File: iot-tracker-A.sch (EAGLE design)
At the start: 22 parts, among them U1 ESP-WROOM-02, U2 TPL5111DDCR, U3 MCP1640T-I_CHY

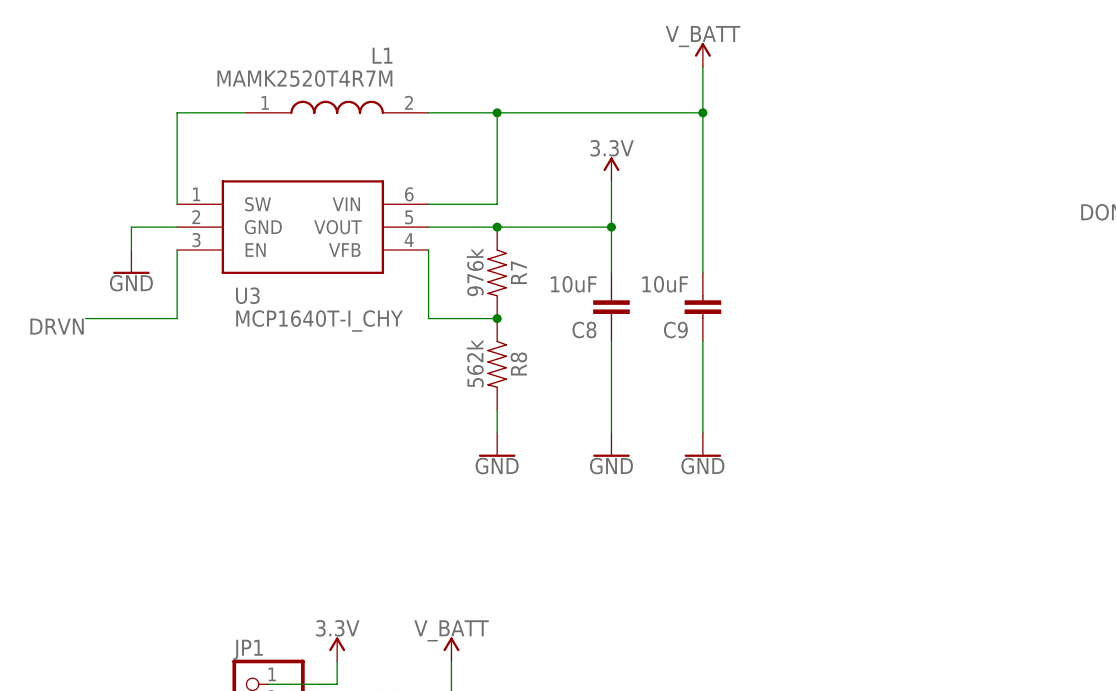
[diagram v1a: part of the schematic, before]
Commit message: Started phasing out the MCP1640 boost converter
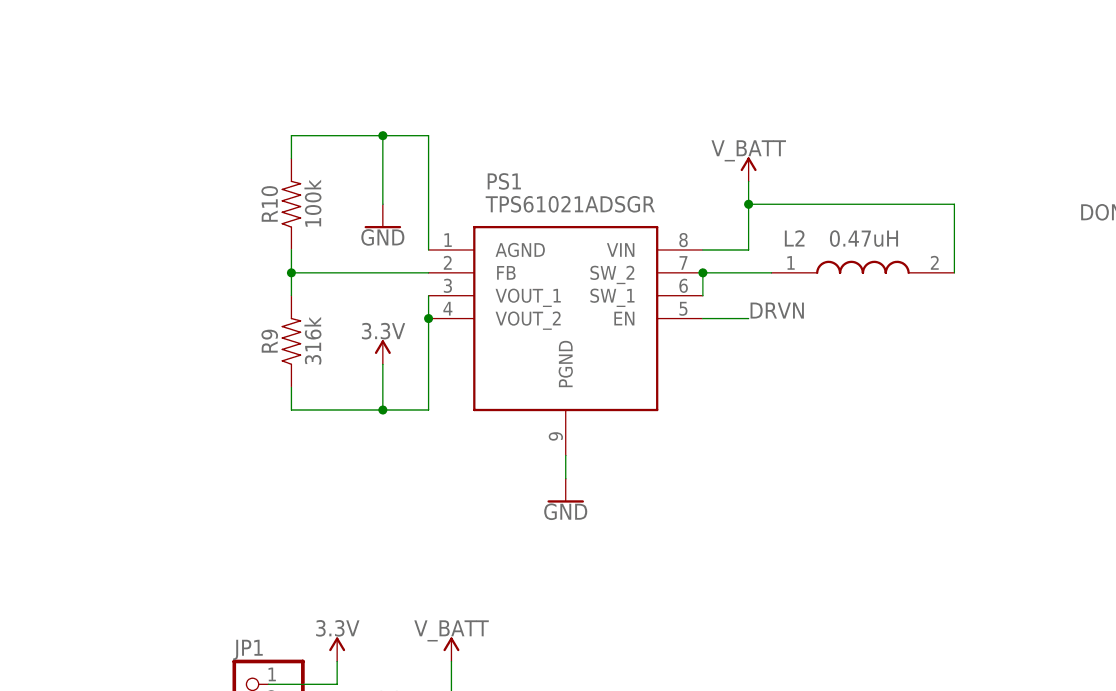
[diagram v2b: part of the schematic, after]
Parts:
- removed C8, C9: 10uF, SparkFun-Capacitors:10UF-0603-6.3V-20%
- removed L1: MAMK2520T4R7M, MAMK2520T4R7M:MAMK2520T4R7M
- removed R7: 976k, SparkFun-Resistors:680OHM-0603-1/10W-5%
- removed R8: 562k, SparkFun-Resistors:680OHM-0603-1/10W-5%
- removed U3: MCP1640T-I_CHY, MCP1640T-I_CHY:MCP1640T-I_CHY
- added L2: 0.47uH, IOT-Tracker-A:DFE252012P-R47M=P2
- added PS1: TPS61021ADSGR, IOT-Tracker-A:TPS61021ADSGR
- added R10: 100k, SparkFun-Resistors:100KOHM-0603-1/10W-1%
- added R9: 316k, SparkFun-Resistors:300KOHM-0603-1/10W-1%
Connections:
- removed net SW: L1.1, U3.SW
- removed net VFB: R7.2, R8.1, U3.VFB
- new net N$1: PS1.FB, R10.1, R9.2
- new net N$3: L2.1, PS1.SW_1, PS1.SW_2
- net 3.3V: now also PS1.VOUT_1, PS1.VOUT_2, R9.1; no longer C8.2, R7.1, U3.VOUT
- net DRVN: now also PS1.EN; no longer U3.EN
- net GND: now also PS1.AGND, PS1.PGND, R10.2; no longer C8.1, C9.1, R8.2, U3.GND
- net V_BATT: now also L2.2, PS1.VIN; no longer C9.2, L1.2, U3.VIN

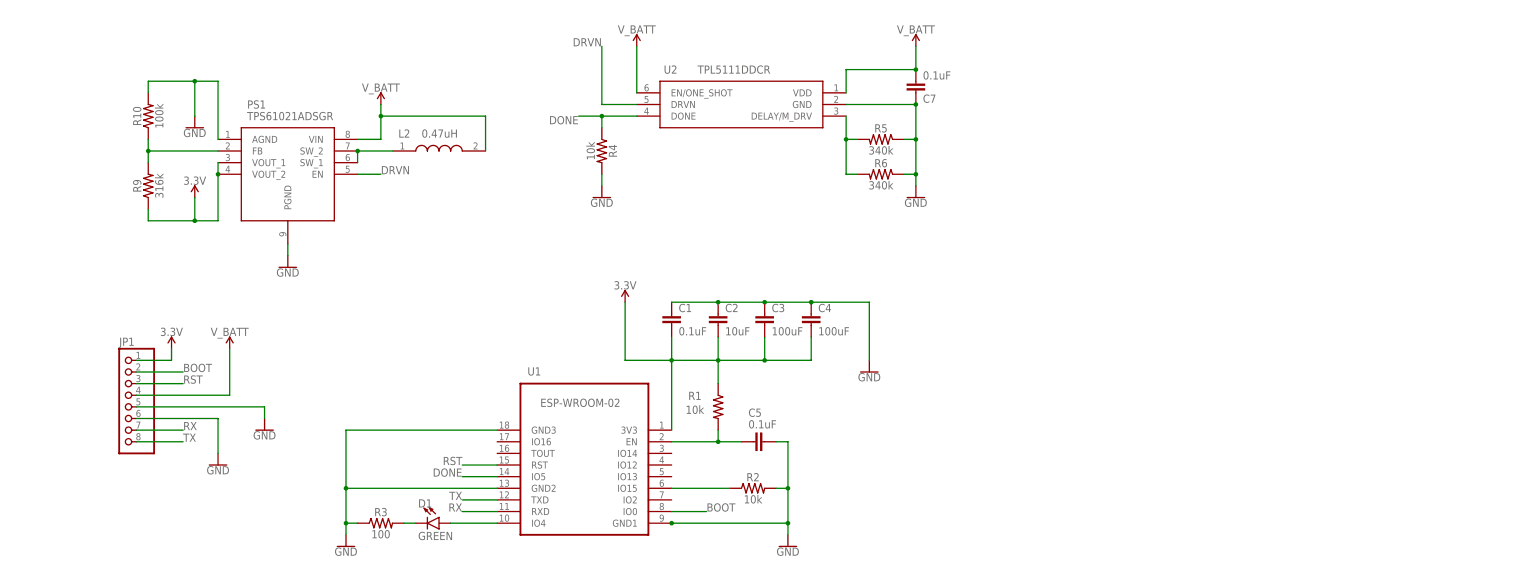
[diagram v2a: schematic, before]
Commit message: Integrated the TPS61021A into the schematic
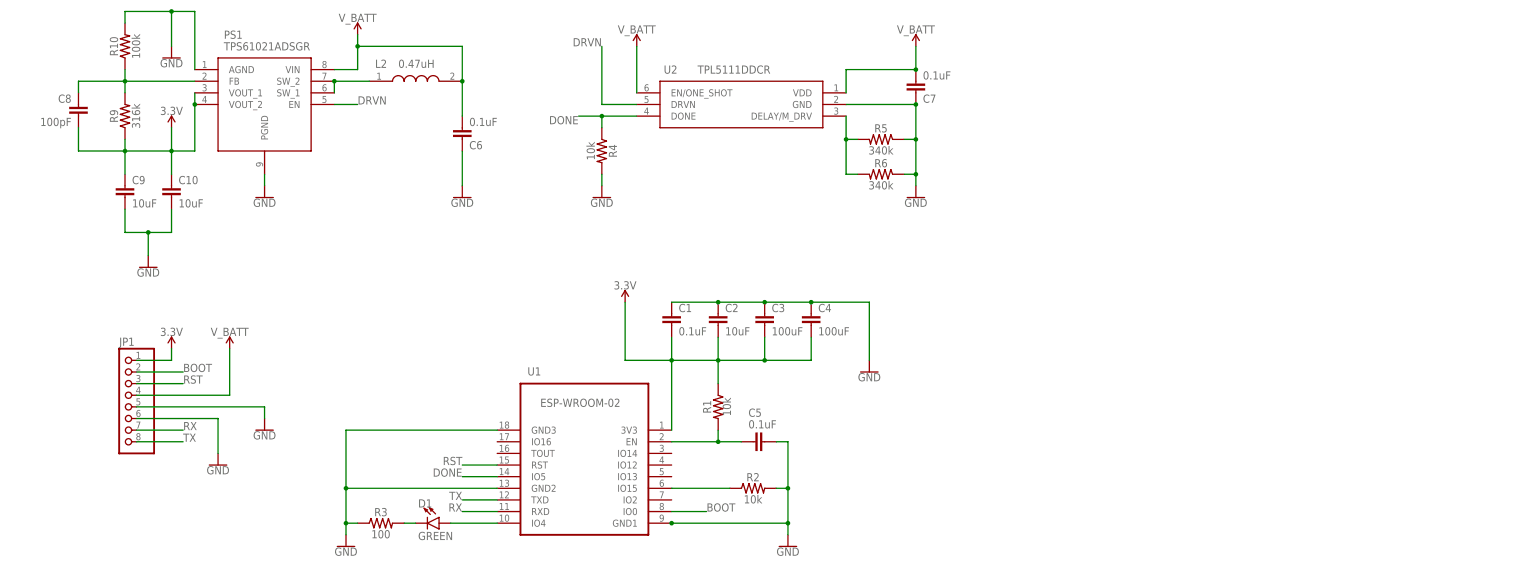
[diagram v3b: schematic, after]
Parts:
- added C10, C9: 10uF, SparkFun-Capacitors:10UF-0603-6.3V-20%
- added C6: 0.1uF, SparkFun-Capacitors:0.1UF-0603-25V-(+80/-20%)
- added C8: 100pF, SparkFun-Capacitors:100PF-0603-50V-5%
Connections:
- net N$3 renamed SW
- net 3.3V: now also C10.1, C8.2, C9.1
- net GND: now also C10.2, C6.1, C9.2
- net N$1: now also C8.1
- net V_BATT: now also C6.2
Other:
- moved on the sheet: L2, PS1, R10, R9

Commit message: Changed bulk capacitors to tantalum; minor component edits
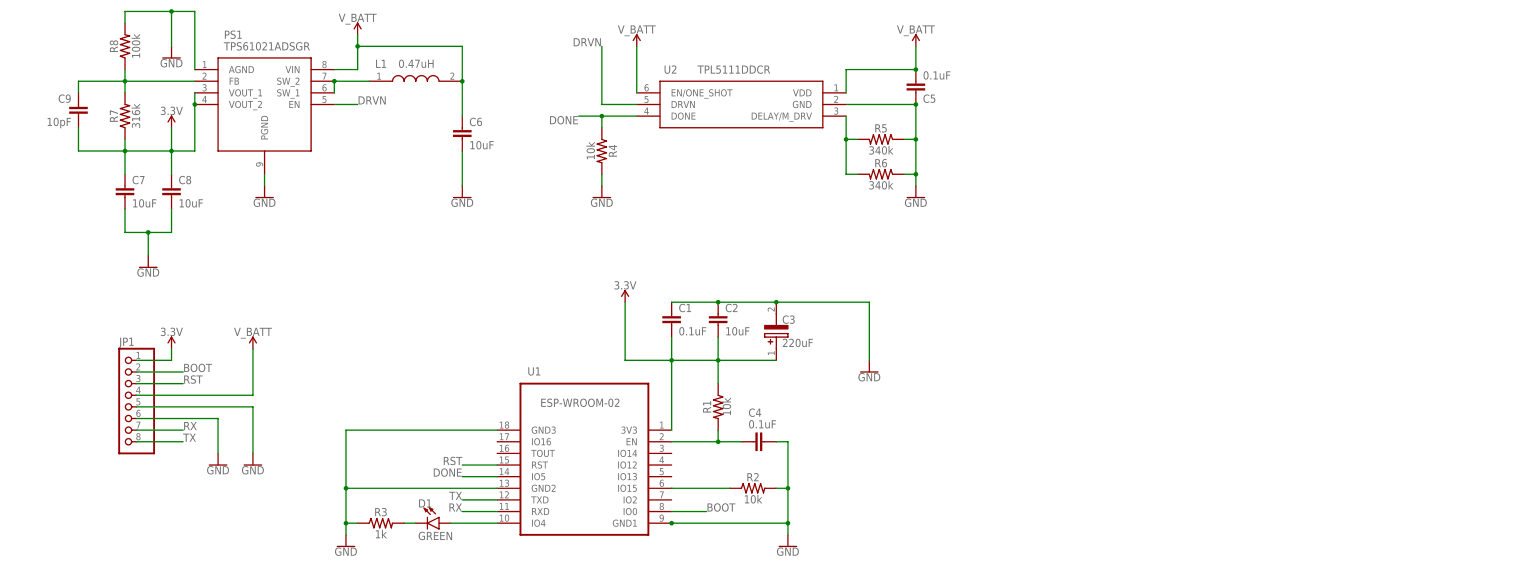
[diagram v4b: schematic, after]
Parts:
- removed C10: 10uF, SparkFun-Capacitors:10UF-0603-6.3V-20%
- C3: value 100uF -> 220uF; device SparkFun-Capacitors:10UF-1206-6.3V-20% -> IOT-Tracker-A:593D227X0010E2TE3
- C4: value 100uF -> 0.1uF; device SparkFun-Capacitors:10UF-1206-6.3V-20% -> SparkFun-Capacitors:0.1UF-0603-25V-(+80/-20%)
- C6, C7: value 0.1uF -> 10uF; device SparkFun-Capacitors:0.1UF-0603-25V-(+80/-20%) -> SparkFun-Capacitors:10UF-0603-6.3V-20%
- C8: value 100pF -> 10uF; device SparkFun-Capacitors:100PF-0603-50V-5% -> SparkFun-Capacitors:10UF-0603-6.3V-20%
- C9: value 10uF -> 10pF; device SparkFun-Capacitors:10UF-0603-6.3V-20% -> SparkFun-Capacitors:10PF-0603-50V-5%
- R3: value 100 -> 1k; device SparkFun-Resistors:100OHM-0603-1/10W-1% -> SparkFun-Resistors:1KOHM-0603-1/10W-1%
- renumbered L2 to L1, R10 to R8, R9 to R7
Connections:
- net 3.3V: now also C3.+, C7.1, C8.1, C9.2; no longer C10.1, C3.2, C4.2, C8.2, C9.1
- net EN: now also C4.2; no longer C5.2
- net GND: now also C3.-, C6.2, C7.2, C8.2; no longer C10.2, C3.1, C6.1, C7.1, C9.2
- net N$1: now also C9.1; no longer C8.1
- net V_BATT: now also C5.2, C6.1; no longer C6.2, C7.2
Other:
- moved on the sheet: C4, C5, C6, C7, C8, C9

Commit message: Started basic board layout
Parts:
- renumbered PS1 to U3
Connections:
- net N$1 renamed FB
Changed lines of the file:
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@@
 <class number="1" name="POWER" width="0.6096" drill="0">
 </class>
-<class number="2" name="SIGNAL" width="0.3048" drill="0">
-<clearance class="2" value="0.3048"/>
+<class number="2" name="SIGNAL" width="0.1524" drill="0">
+<clearance class="2" value="0.1524"/>
 </class>
 <class number="3" name="DATA" width="0" drill="0">
-<clearance class="3" value="0.3048"/>
+<clearance class="3" value="0.1524"/>
 </class>
 </classes>
@@
 <part name="GND11" library="SparkFun-PowerSymbols" library_urn="urn:adsk.eagle:library:530" deviceset="GND" device=""/>
 <part name="GND1" library="SparkFun-PowerSymbols" library_urn="urn:adsk.eagle:library:530" deviceset="GND" device=""/>
-<part name="PS1" library="IOT-Tracker-A" deviceset="TPS61021ADSGR" device=""/>
+<part name="U3" library="IOT-Tracker-A" deviceset="TPS61021ADSGR" device=""/>
 <part name="SUPPLY6" library="SparkFun-PowerSymbols" library_urn="urn:adsk.eagle:library:530" deviceset="V_BATT" device=""/>
 <part name="GND10" library="SparkFun-PowerSymbols" library_urn="urn:adsk.eagle:library:530" deviceset="GND" device=""/>
@@
 <attribute name="VALUE" x="-48.26" y="-38.354" size="1.778" layer="96" align="top-center"/>
 </instance>
-<instance part="PS1" gate="G$1" x="-60.96" y="48.26" smashed="yes">
+<instance part="U3" gate="G$1" x="-60.96" y="48.26" smashed="yes">
 <attribute name="NAME" x="-54.61" y="55.88" size="1.778" layer="95" align="center-left"/>
 <attribute name="VALUE" x="-54.61" y="53.34" size="1.778" layer="96" align="center-left"/>
@@
 </segment>
 <segment>
-<pinref part="PS1" gate="G$1" pin="PGND"/>
+<pinref part="U3" gate="G$1" pin="PGND"/>
 <pinref part="GND10" gate="1" pin="GND"/>
 <wire x1="-45.72" y1="25.4" x2="-45.72" y2="22.86" width="0.1524" layer="91"/>
@@
 <pinref part="R8" gate="G$1" pin="2"/>
 <wire x1="-76.2" y1="58.42" x2="-76.2" y2="60.96" width="0.1524" layer="91"/>
-<pinref part="PS1" gate="G$1" pin="AGND"/>
+<pinref part="U3" gate="G$1" pin="AGND"/>
 <wire x1="-76.2" y1="60.96" x2="-66.04" y2="60.96" width="0.1524" layer="91"/>
 <wire x1="-66.04" y1="60.96" x2="-60.96" y2="60.96" width="0.1524" layer="91"/>
@@
 </segment>
 <segment>
-<pinref part="PS1" gate="G$1" pin="EN"/>
+<pinref part="U3" gate="G$1" pin="EN"/>
 <wire x1="-30.48" y1="40.64" x2="-25.4" y2="40.64" width="0.1524" layer="91"/>
 <label x="-25.4" y="40.64" size="1.778" layer="95"/>
@@
 </segment>
 <segment>
-<pinref part="PS1" gate="G$1" pin="VOUT_1"/>
+<pinref part="U3" gate="G$1" pin="VOUT_1"/>
 <wire x1="-60.96" y1="43.18" x2="-60.96" y2="40.64" width="0.1524" layer="91"/>
 <wire x1="-60.96" y1="40.64" x2="-60.96" y2="30.48" width="0.1524" layer="91"/>
@@
 <wire x1="-66.04" y1="30.48" x2="-76.2" y2="30.48" width="0.1524" layer="91"/>
 <wire x1="-76.2" y1="30.48" x2="-76.2" y2="33.02" width="0.1524" layer="91"/>
-<pinref part="PS1" gate="G$1" pin="VOUT_2"/>
+<pinref part="U3" gate="G$1" pin="VOUT_2"/>
 <junction x="-60.96" y="40.64"/>
 <wire x1="-66.04" y1="30.48" x2="-66.04" y2="35.56" width="0.1524" layer="91"/>
@@
 </segment>
 <segment>
-<pinref part="PS1" gate="G$1" pin="VIN"/>
+<pinref part="U3" gate="G$1" pin="VIN"/>
 <pinref part="SUPPLY6" gate="G$1" pin="V_BATT"/>
 <wire x1="-30.48" y1="48.26" x2="-25.4" y2="48.26" width="0.1524" layer="91"/>
@@
 </segment>
 </net>
-<net name="N$1" class="0">
-<segment>
-<pinref part="PS1" gate="G$1" pin="FB"/>
+<net name="FB" class="0">
+<segment>
+<pinref part="U3" gate="G$1" pin="FB"/>
 <wire x1="-60.96" y1="45.72" x2="-76.2" y2="45.72" width="0.1524" layer="91"/>
 <pinref part="R8" gate="G$1" pin="1"/>
@@
 <net name="SW" class="0">
 <segment>
-<pinref part="PS1" gate="G$1" pin="SW_1"/>
-<pinref part="PS1" gate="G$1" pin="SW_2"/>
+<pinref part="U3" gate="G$1" pin="SW_1"/>
+<pinref part="U3" gate="G$1" pin="SW_2"/>
 <wire x1="-30.48" y1="43.18" x2="-30.48" y2="45.72" width="0.1524" layer="91"/>
 <pinref part="L1" gate="G$1" pin="1"/>

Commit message: Routed everything but GND
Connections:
- net RX: now also JP1.8; no longer JP1.7
- net TX: now also JP1.7; no longer JP1.8
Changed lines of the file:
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@@
 </segment>
 <segment>
-<pinref part="JP1" gate="A" pin="7"/>
-<wire x1="-73.66" y1="-30.48" x2="-63.5" y2="-30.48" width="0.1524" layer="91"/>
-<label x="-63.5" y="-30.48" size="1.778" layer="95"/>
+<pinref part="JP1" gate="A" pin="8"/>
+<wire x1="-73.66" y1="-33.02" x2="-63.5" y2="-33.02" width="0.1524" layer="91"/>
+<label x="-63.5" y="-33.02" size="1.778" layer="95"/>
 </segment>
 </net>
@@
 </segment>
 <segment>
-<pinref part="JP1" gate="A" pin="8"/>
-<wire x1="-73.66" y1="-33.02" x2="-63.5" y2="-33.02" width="0.1524" layer="91"/>
-<label x="-63.5" y="-33.02" size="1.778" layer="95"/>
+<pinref part="JP1" gate="A" pin="7"/>
+<wire x1="-73.66" y1="-30.48" x2="-63.5" y2="-30.48" width="0.1524" layer="91"/>
+<label x="-63.5" y="-30.48" size="1.778" layer="95"/>
 </segment>
 </net>
